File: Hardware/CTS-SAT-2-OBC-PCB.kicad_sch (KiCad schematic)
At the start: 0 parts

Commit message: Finish schematic v1
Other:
- sheet Connectors ports: added MISO_USART2_RX, MOSI_USART2_TX; removed ADCS_UART2_RX, ADCS_UART2_TX
- sheet STM32 ports: added I2C2_SCL, I2C2_SDA; removed I2C1_SCL, I2C1_SDA
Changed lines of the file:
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@@
+	(wire
+		(pts
+			(xy 203.2 140.97) (xy 265.43 140.97)
+		)
+		(stroke
+			(width 0)
+			(type default)
+		)
+	)
 	(wire
 		(pts
@@
 	(wire
 		(pts
+			(xy 203.2 135.89) (xy 265.43 135.89)
+		)
+		(stroke
+			(width 0)
+			(type default)
+		)
+	)
+	(wire
+		(pts
 			(xy 203.2 87.63) (xy 265.43 87.63)
 		)
@@
 	(wire
 		(pts
+			(xy 203.2 133.35) (xy 265.43 133.35)
+		)
+		(stroke
+			(width 0)
+			(type default)
+		)
+	)
+	(wire
+		(pts
 			(xy 203.2 187.96) (xy 265.43 187.96)
 		)
@@
 	(wire
 		(pts
+			(xy 203.2 143.51) (xy 265.43 143.51)
+		)
+		(stroke
+			(width 0)
+			(type default)
+		)
+	)
+	(wire
+		(pts
 			(xy 203.2 180.34) (xy 265.43 180.34)
 		)
@@
 		(pts
 			(xy 115.57 111.76) (xy 154.94 111.76)
-		)
-		(stroke
-			(width 0)
-			(type default)
-		)
-	)
-	(wire
-		(pts
-			(xy 203.2 143.51) (xy 265.43 143.51)
-		)
-		(stroke
-			(width 0)
-			(type default)
-		)
-	)
-	(wire
-		(pts
-			(xy 203.2 140.97) (xy 265.43 140.97)
 		)
 		(stroke
@@
 			)
 		)
-		(pin "ADCS_UART2_RX" input
-			(at 265.43 125.73 180)
-			(effects
-				(font
-					(size 1.27 1.27)
-				)
-				(justify left)
-			)
-		)
-		(pin "ADCS_UART2_TX" output
-			(at 265.43 128.27 180)
-			(effects
-				(font
-					(size 1.27 1.27)
-				)
-				(justify left)
-			)
-		)
 		(pin "CAM_EN" input
 			(at 265.43 168.91 180)
@@
 		)
 		(pin "MISO_UART4_RX" output
+			(at 265.43 143.51 180)
+			(effects
+				(font
+					(size 1.27 1.27)
+				)
+				(justify left)
+			)
+		)
+		(pin "MOSI_UART4_TX" input
 			(at 265.43 140.97 180)
-			(effects
-				(font
-					(size 1.27 1.27)
-				)
-				(justify left)
-			)
-		)
-		(pin "MOSI_UART4_TX" input
-			(at 265.43 143.51 180)
 			(effects
 				(font
@@
 		(pin "RP2040_~{BOOTSEL}" output
 			(at 265.43 60.96 180)
+			(effects
+				(font
+					(size 1.27 1.27)
+				)
+				(justify left)
+			)
+		)
+		(pin "MOSI_USART2_TX" input
+			(at 265.43 125.73 180)
+			(effects
+				(font
+					(size 1.27 1.27)
+				)
+				(justify left)
+			)
+		)
+		(pin "MISO_USART2_RX" output
+			(at 265.43 128.27 180)
 			(effects
 				(font
@@
 			)
 		)
-		(pin "I2C1_SDA" bidirectional
-			(at 203.2 85.09 0)
-			(effects
-				(font
-					(size 1.27 1.27)
-				)
-				(justify right)
-			)
-		)
-		(pin "I2C1_SCL" bidirectional
-			(at 203.2 87.63 0)
-			(effects
-				(font
-					(size 1.27 1.27)
-				)
-				(justify right)
-			)
-		)
 		(pin "MISO_UART4_RX" input
 			(at 203.2 143.51 0)
@@
 			(effects
 				(font
+					(size 1.27 1.27)
+				)
+				(justify right)
+			)
+		)
+		(pin "I2C2_SCL" bidirectional
+			(at 203.2 87.63 0)
+			(effects
+				(font
+					(size 1.27 1.27)
+				)
+				(justify right)
+			)
+		)
+		(pin "I2C2_SDA" bidirectional
+			(at 203.2 85.09 0)
+			(effects
+				(font

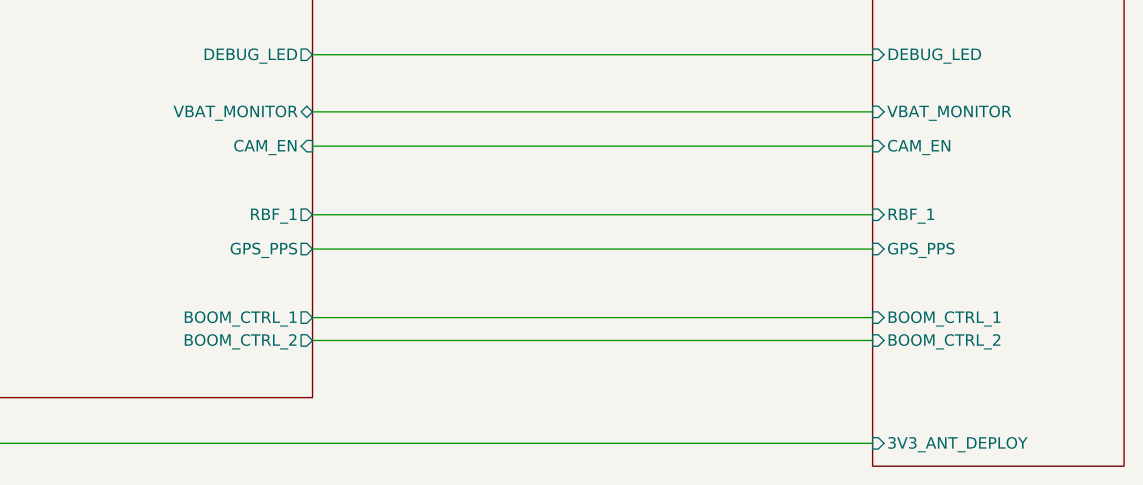
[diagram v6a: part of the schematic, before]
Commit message: Add IOC and second burnwire connector
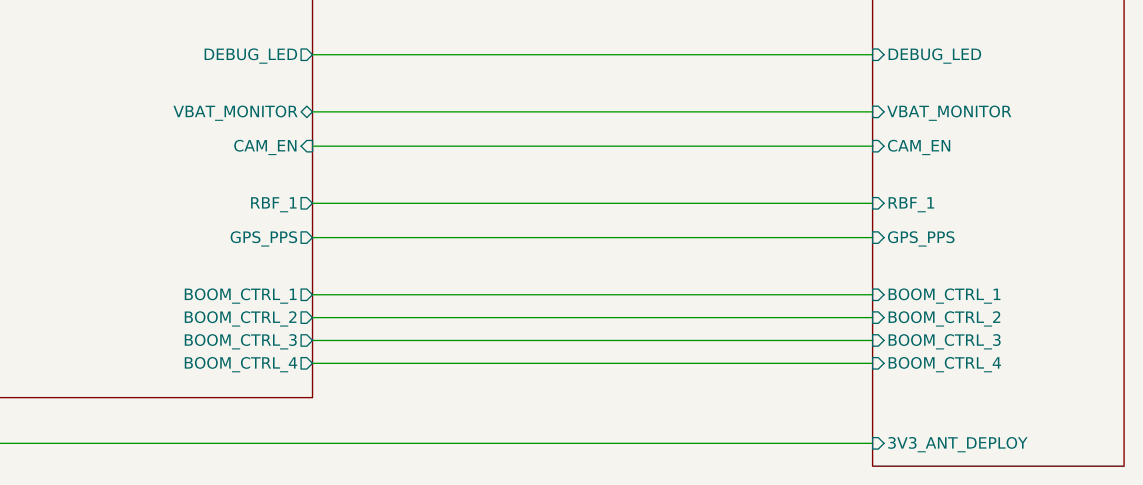
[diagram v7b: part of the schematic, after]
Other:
- sheet Connectors ports: added BOOM_CTRL_3, BOOM_CTRL_4; removed none
- sheet STM32 ports: added BOOM_CTRL_3, BOOM_CTRL_4; removed none
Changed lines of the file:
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@@
+	(wire
+		(pts
+			(xy 203.2 187.96) (xy 265.43 187.96)
+		)
+		(stroke
+			(width 0)
+			(type default)
+		)
+	)
+	(wire
+		(pts
+			(xy 203.2 69.85) (xy 265.43 69.85)
+		)
+		(stroke
+			(width 0)
+			(type default)
+		)
+	)
+	(wire
+		(pts
+			(xy 203.2 118.11) (xy 219.71 118.11)
+		)
+		(stroke
+			(width 0)
+			(type default)
+		)
+	)
+	(wire
+		(pts
+			(xy 203.2 148.59) (xy 265.43 148.59)
+		)
+		(stroke
+			(width 0)
+			(type default)
+		)
+	)
+	(wire
+		(pts
+			(xy 203.2 104.14) (xy 265.43 104.14)
+		)
+		(stroke
+			(width 0)
+			(type default)
+		)
+	)
+	(wire
+		(pts
+			(xy 142.24 142.24) (xy 154.94 142.24)
+		)
+		(stroke
+			(width 0)
+			(type default)
+		)
+	)
+	(wire
+		(pts
+			(xy 203.2 110.49) (xy 219.71 110.49)
+		)
+		(stroke
+			(width 0)
+			(type default)
+		)
+	)
+	(wire
+		(pts
+			(xy 203.2 135.89) (xy 265.43 135.89)
+		)
+		(stroke
+			(width 0)
+			(type default)
+		)
+	)
+	(wire
+		(pts
+			(xy 203.2 87.63) (xy 265.43 87.63)
+		)
+		(stroke
+			(width 0)
+			(type default)
+		)
+	)
 	(wire
 		(pts
@@
 	(wire
 		(pts
-			(xy 203.2 69.85) (xy 265.43 69.85)
-		)
-		(stroke
-			(width 0)
-			(type default)
-		)
-	)
-	(wire
-		(pts
-			(xy 203.2 118.11) (xy 219.71 118.11)
-		)
-		(stroke
-			(width 0)
-			(type default)
-		)
-	)
-	(wire
-		(pts
-			(xy 203.2 148.59) (xy 265.43 148.59)
-		)
-		(stroke
-			(width 0)
-			(type default)
-		)
-	)
-	(wire
-		(pts
-			(xy 203.2 104.14) (xy 265.43 104.14)
-		)
-		(stroke
-			(width 0)
-			(type default)
-		)
-	)
-	(wire
-		(pts
-			(xy 142.24 142.24) (xy 154.94 142.24)
-		)
-		(stroke
-			(width 0)
-			(type default)
-		)
-	)
-	(wire
-		(pts
-			(xy 203.2 110.49) (xy 219.71 110.49)
-		)
-		(stroke
-			(width 0)
-			(type default)
-		)
-	)
-	(wire
-		(pts
-			(xy 203.2 135.89) (xy 265.43 135.89)
-		)
-		(stroke
-			(width 0)
-			(type default)
-		)
-	)
-	(wire
-		(pts
-			(xy 203.2 87.63) (xy 265.43 87.63)
-		)
-		(stroke
-			(width 0)
-			(type default)
-		)
-	)
-	(wire
-		(pts
 			(xy 115.57 60.96) (xy 265.43 60.96)
 		)
@@
 	(wire
 		(pts
+			(xy 203.2 193.04) (xy 265.43 193.04)
+		)
+		(stroke
+			(width 0)
+			(type default)
+		)
+	)
+	(wire
+		(pts
 			(xy 203.2 85.09) (xy 265.43 85.09)
 		)
@@
 	(wire
 		(pts
-			(xy 203.2 187.96) (xy 265.43 187.96)
-		)
-		(stroke
-			(width 0)
-			(type default)
-		)
-	)
-	(wire
-		(pts
-			(xy 203.2 176.53) (xy 265.43 176.53)
+			(xy 203.2 185.42) (xy 265.43 185.42)
+		)
+		(stroke
+			(width 0)
+			(type default)
+		)
+	)
+	(wire
+		(pts
+			(xy 203.2 175.26) (xy 265.43 175.26)
 		)
 		(stroke
@@
 	(wire
 		(pts
-			(xy 203.2 180.34) (xy 265.43 180.34)
+			(xy 203.2 179.07) (xy 265.43 179.07)
 		)
 		(stroke
@@
 		)
 		(pin "RBF_1" input
-			(at 265.43 176.53 180)
+			(at 265.43 175.26 180)
 			(effects
 				(font
@@
 		)
 		(pin "GPS_PPS" input
-			(at 265.43 180.34 180)
+			(at 265.43 179.07 180)
 			(effects
 				(font
@@
 		)
 		(pin "BOOM_CTRL_1" input
+			(at 265.43 185.42 180)
+			(effects
+				(font
+					(size 1.27 1.27)
+				)
+				(justify left)
+			)
+		)
+		(pin "BOOM_CTRL_2" input
 			(at 265.43 187.96 180)
-			(effects
-				(font
-					(size 1.27 1.27)
-				)
-				(justify left)
-			)
-		)
-		(pin "BOOM_CTRL_2" input
-			(at 265.43 190.5 180)
 			(effects
 				(font
@@
 		(pin "MISO_USART2_RX" output
 			(at 265.43 128.27 180)
+			(effects
+				(font
+					(size 1.27 1.27)
+				)
+				(justify left)
+			)
+		)
+		(pin "BOOM_CTRL_3" input
+			(at 265.43 190.5 180)
+			(effects
+				(font
+					(size 1.27 1.27)
+				)
+				(justify left)
+			)
+		)
+		(pin "BOOM_CTRL_4" input
+			(at 265.43 193.04 180)
 			(effects
 				(font
@@
 		)
 		(pin "GPS_PPS" output
-			(at 203.2 180.34 0)
+			(at 203.2 179.07 0)
 			(effects
 				(font
@@
 		)
 		(pin "RBF_1" output
-			(at 203.2 176.53 0)
+			(at 203.2 175.26 0)
 			(effects
 				(font
@@
 		)
 		(pin "BOOM_CTRL_1" output
+			(at 203.2 185.42 0)
+			(effects
+				(font
+					(size 1.27 1.27)
+				)
+				(justify right)
+			)
+		)
+		(pin "BOOM_CTRL_2" output
 			(at 203.2 187.96 0)
-			(effects
-				(font
-					(size 1.27 1.27)
-				)
-				(justify right)
-			)
-		)
-		(pin "BOOM_CTRL_2" output
-			(at 203.2 190.5 0)
 			(effects
 				(font
@@
 			(effects
 				(font
+					(size 1.27 1.27)
+				)
+				(justify right)
+			)
+		)
+		(pin "BOOM_CTRL_3" output
+			(at 203.2 190.5 0)
+			(effects
+				(font
+					(size 1.27 1.27)
+				)
+				(justify right)
+			)
+		)
+		(pin "BOOM_CTRL_4" output
+			(at 203.2 193.04 0)
+			(effects
+				(font

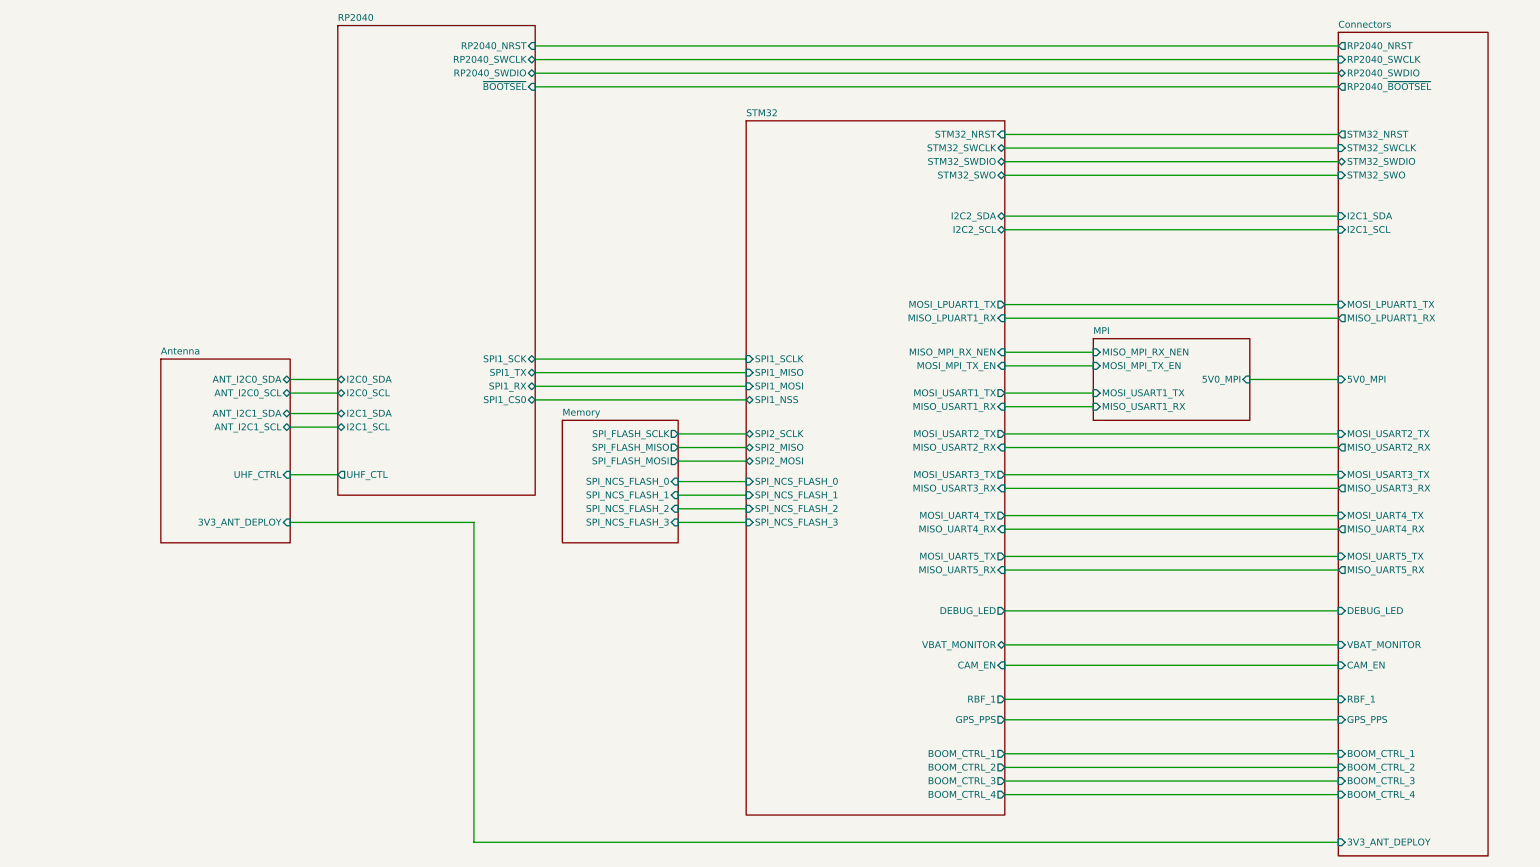
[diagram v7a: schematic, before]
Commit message: Update schematic to allow using STM32 alone
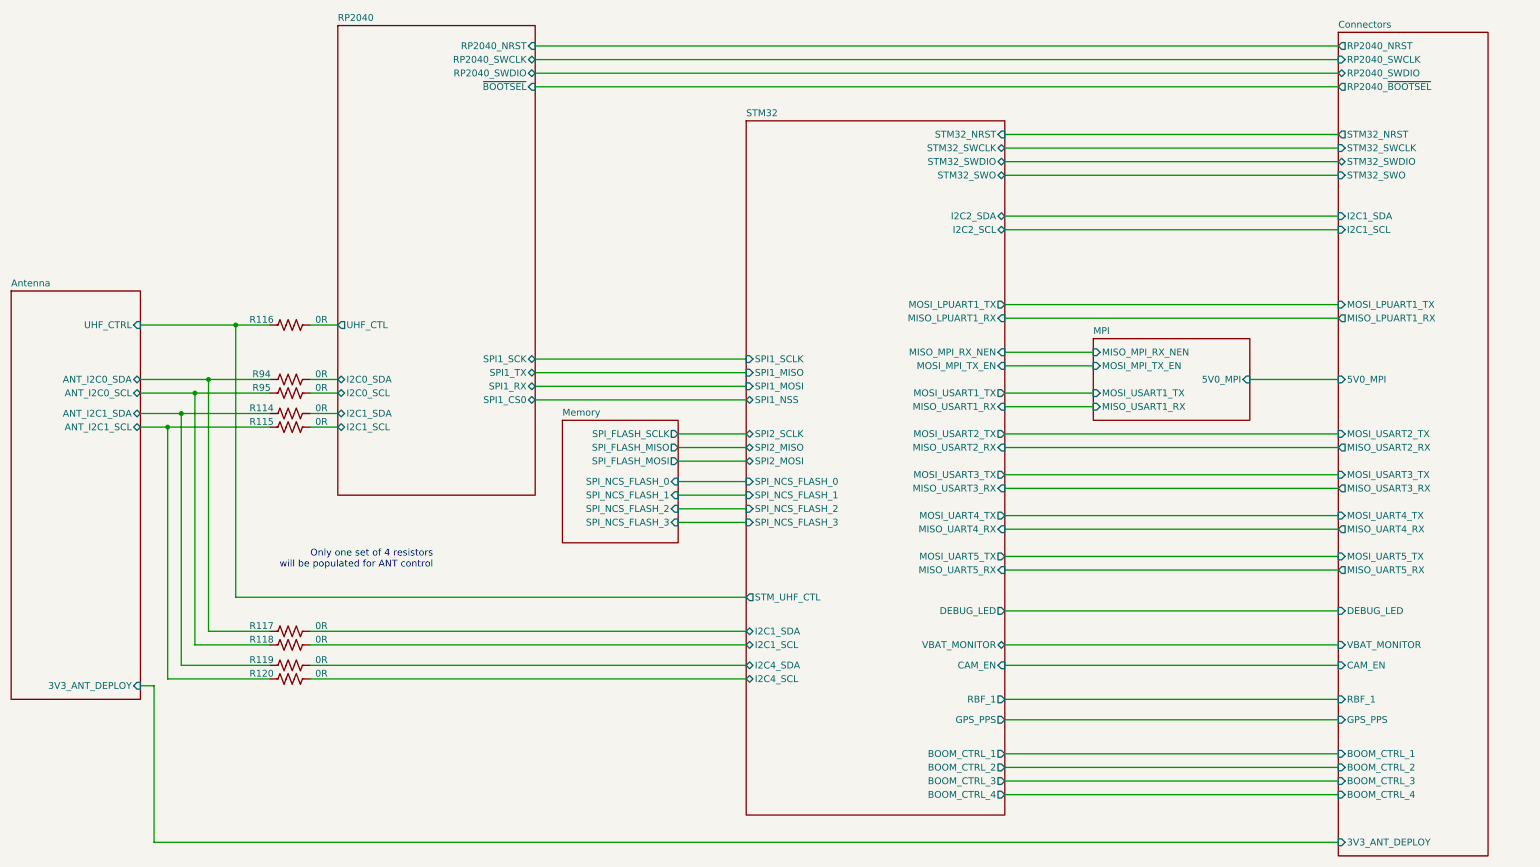
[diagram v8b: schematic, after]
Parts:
- added R114, R115, R116, R117, R118, R119, R120, R94, R95: 0R, Resistor_SMD:R_0603_1608Metric, symbol Device:R_US
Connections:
- net Antenna/ANT_I2C0_SCL: now also R118.1, R95.1
- net Antenna/ANT_I2C0_SDA: now also R117.1, R94.1
- net Antenna/ANT_I2C1_SCL: now also R115.1, R120.1
- net Antenna/ANT_I2C1_SDA: now also R114.1, R119.1
- net Antenna/UHF_CTRL: now also R116.1
- new net RP2040/I2C0_SCL: R95.2
- new net RP2040/I2C0_SDA: R94.2
- new net RP2040/I2C1_SCL: R115.2
- new net RP2040/I2C1_SDA: R114.2
- new net RP2040/UHF_CTL: R116.2
- new net STM32/I2C1_SCL: R118.2
- new net STM32/I2C1_SDA: R117.2
- new net STM32/I2C4_SCL: R120.2
- new net STM32/I2C4_SDA: R119.2
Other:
- sheet STM32 ports: added I2C1_SCL, I2C1_SDA, I2C4_SCL, I2C4_SDA, STM_UHF_CTL; removed none
- note added: "Only one set of 4 resistors will be populated for ANT control"
